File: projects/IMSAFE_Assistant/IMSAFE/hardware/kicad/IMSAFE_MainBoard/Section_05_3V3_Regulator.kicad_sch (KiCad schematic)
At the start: 0 parts

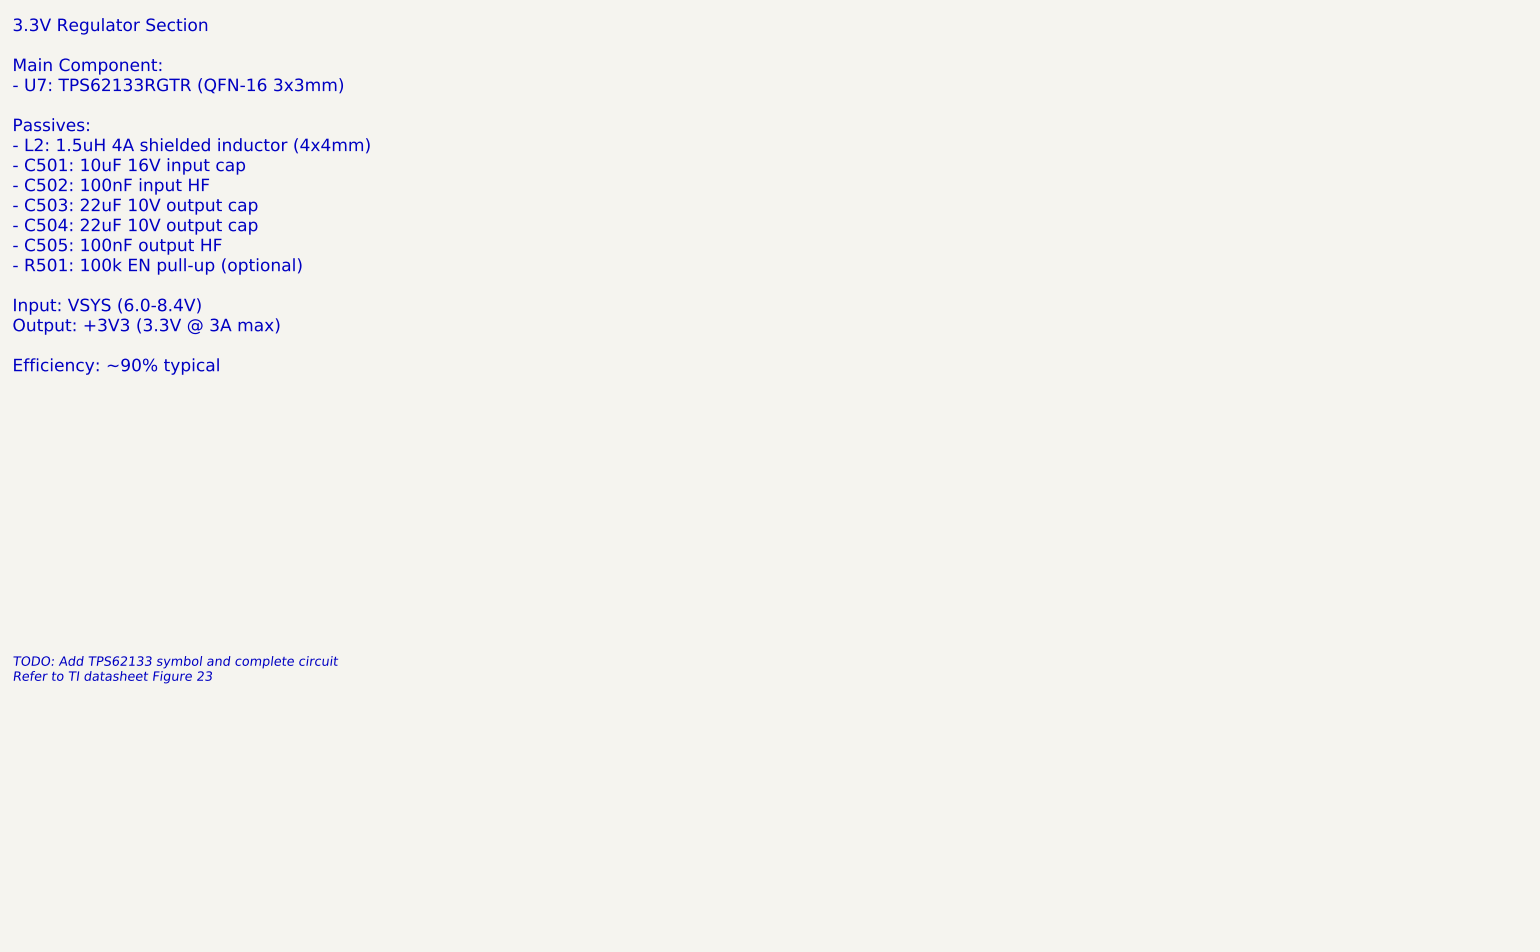
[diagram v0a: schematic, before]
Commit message: Add Sections 05-06: 3.3V and 5V buck regulators
Section 05 - TPS62133 (3.3V Fixed):
- 3A synchronous buck converter
- Input: VSYS (6-8.4V), Output: 3.3V
- Components: L2 (1.5µH), C501-C505, R501 (EN pull-up)
- Powers MCU and digital peripherals

Section 06 - TPS62130 (5V Adjustable):
- 3A synchronous buck converter with FB divider
- Input: VSYS, Output: 5.09V (R601=100k, R602=24.3k)
- Components: L3 (1.5µH), C601-C605, R601-R603
- Powers WS2812B LEDs, display, buzzer

Co-Authored-By: Claude Opus 4.5 <noreply@anthropic.com>
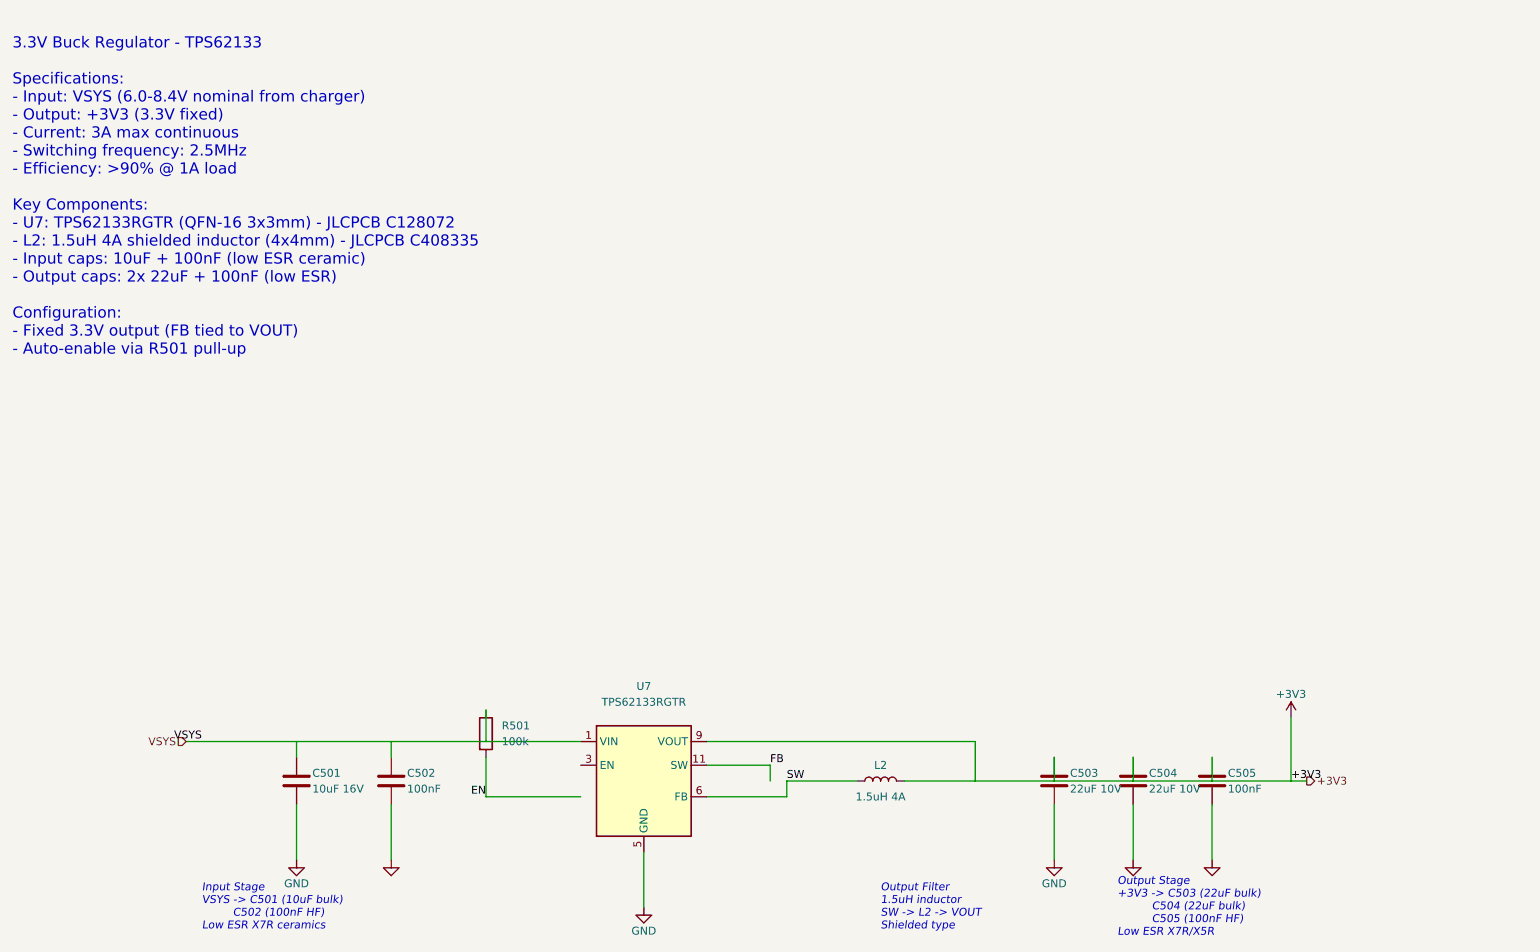
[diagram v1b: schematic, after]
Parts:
- added C501: 10uF 16V, Capacitor_SMD:C_0805_2012Metric, symbol Device:C
- added C502, C505: 100nF, Capacitor_SMD:C_0603_1608Metric, symbol Device:C
- added C503, C504: 22uF 10V, Capacitor_SMD:C_0805_2012Metric, symbol Device:C
- added L2: 1.5uH 4A, Inductor_SMD:L_4x4mm_H2.5mm, symbol Device:L
- added R501: 100k, Resistor_SMD:R_0603_1608Metric, symbol Device:R
- added U7: TPS62133RGTR, Package_DFN_QFN:QFN-16-1EP_3x3mm_P0.5mm_EP1.8x1.8mm, symbol Regulator:TPS62133RGTR
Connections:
- new net +3V3: C503.1, C504.1, C505.1, L2.2, U7.9 (VOUT)
- new net EN: R501.2
- new net FB: U7.11 (SW)
- new net GND: C501.2, C502.2, C503.2, C504.2, C505.2, U7.5 (GND)
- new net SW: L2.1, U7.6 (FB)
- new net VSYS: C501.1, C502.1, R501.1, U7.1 (VIN)
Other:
- note added: "3.3V Buck Regulator - TPS62133 Specifications: - Input: VSYS (6.0-8.4V nominal from charger) - Output: +3V3 (3.3V fixed) - Current: 3A max continuous - Switching frequency: 2.5MHz - Efficiency: >90% @ 1A load Key Components: - U7: TPS62133RGTR (QFN-16 3x3mm) - JLCPCB C128072 - L2: 1.5uH 4A shielded inductor (4x4mm) - JLCPCB C408335 - Input caps: 10uF + 100nF (low ESR ceramic) - Output caps: 2x 22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"
- note added: "Input Stage VSYS -> C501 (10uF bulk) C502 (100nF HF) Low ESR X7R ceramics"
- note added: "Output Filter 1.5uH inductor SW -> L2 -> VOUT Shielded type"
- note added: "Output Stage +3V3 -> C503 (22uF bulk) C504 (22uF bulk) C505 (100nF HF) Low ESR X7R/X5R"
- note removed: "3.3V Regulator Section Main Component: - U7: TPS62133RGTR (QFN-16 3x3mm) Passives: - L2: 1.5uH 4A shielded inductor (4x4mm) - C501: 10uF 16V input cap - C502: 100nF input HF - C503: 22uF 10V output cap - C504: 22uF 10V output cap - C505: 100nF output HF - R501: 100k EN pull-up (optional) Input: VSYS (6.0-8.4V) Output: +3V3 (3.3V @ 3A max) Efficiency: ~90% typical"
- note removed: "TODO: Add TPS62133 symbol and complete circuit Refer to TI datasheet Figure 23"

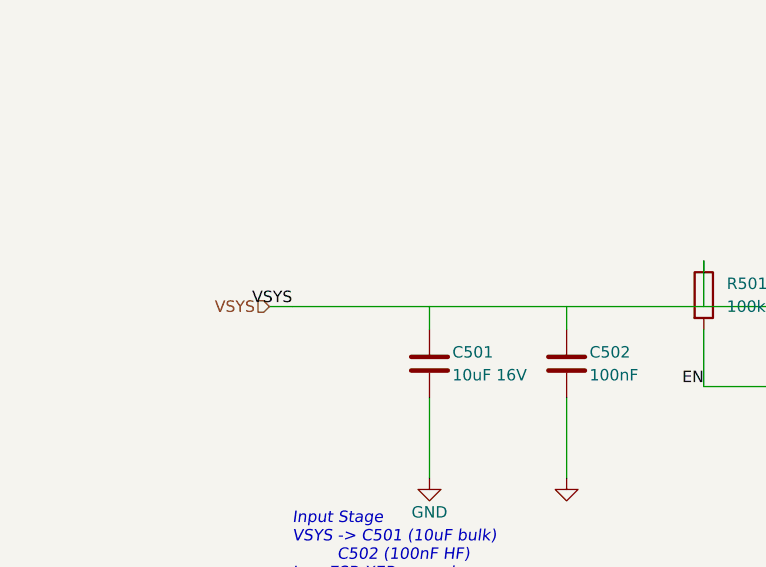
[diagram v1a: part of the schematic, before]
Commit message: Fix Section 06 FB divider for correct 5V output
- Change R602 from 24.3k to 19.1k (JLCPCB C25947)
- Corrects output voltage from 4.09V to 5.03V
- Update schematic text annotations with correct calculations
- Update design-rationale.md to reflect the fix
- Add PWR_FLAG symbols to Sections 04, 05, 06 for ERC compliance

Co-Authored-By: Claude Opus 4.5 <noreply@anthropic.com>
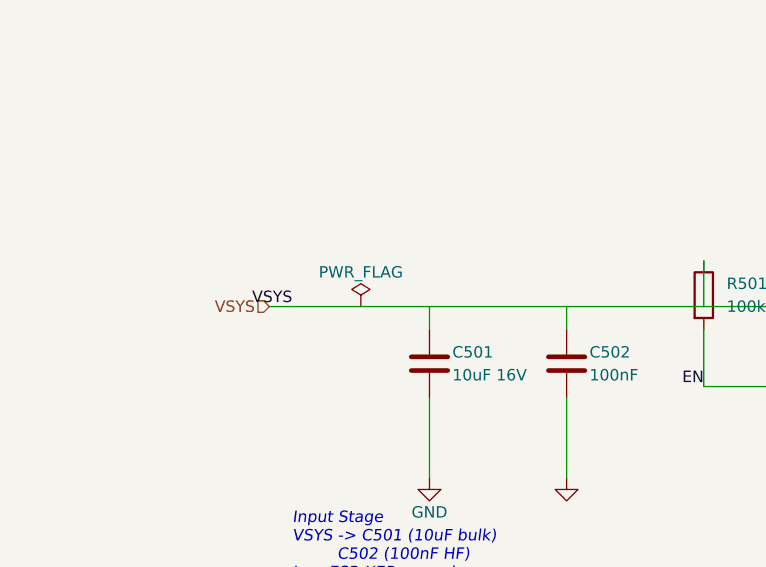
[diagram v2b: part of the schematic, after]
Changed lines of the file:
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@@
 	(wire (pts (xy 53.34 113.03) (xy 55.88 113.03)) (stroke (width 0) (type default)) (uuid "w-hl-vsys"))
 	(wire (pts (xy 231.14 119.38) (xy 233.68 119.38)) (stroke (width 0) (type default)) (uuid "w-hl-3v3"))
+	(symbol (lib_id "power:PWR_FLAG") (at 63.5 113.03 0) (unit 1)
+		(exclude_from_sim no) (in_bom yes) (on_board yes) (dnp no)
+		(uuid "pwr-flag-vsys")
+		(property "Reference" "#FLG0501" (at 63.5 111.125 0) (effects (font (size 1.27 1.27)) hide))
+		(property "Value" "PWR_FLAG" (at 63.5 109.22 0) (effects (font (size 1.27 1.27))))
+		(property "Footprint" "" (at 63.5 113.03 0) (effects (font (size 1.27 1.27)) hide))
+		(property "Datasheet" "~" (at 63.5 113.03 0) (effects (font (size 1.27 1.27)) hide))
+		(pin "1" (uuid "pwr-flag-vsys-p1"))
+		(instances (project "IMSAFE_MainBoard" (path "/sec05-0001-0002-0003-000000000001" (reference "#FLG0501") (unit 1))))
+	)
 	(sheet_instances (path "/" (page "1")))
 )

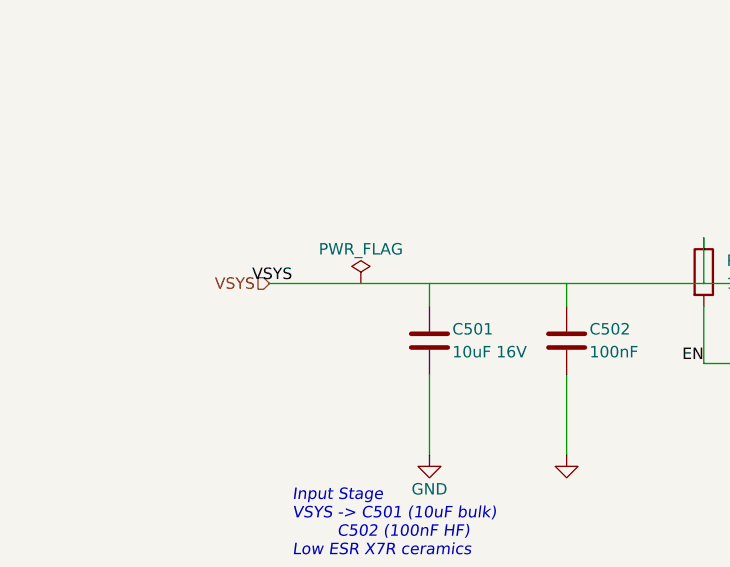
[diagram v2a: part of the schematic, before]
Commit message: Fix ERC errors across multiple schematic sections
- Section_04_BMS: Add VSYS hierarchical label for root schematic connection
- Section_05/06 Regulators: Add PWR_FLAG wire and junction to VSYS net
- Section_07_Barometric: Connect BMP390 SCK pin to GND for I2C mode
- Section_14_IO_Expander: Add no-connect symbols for unused MCP23017 GPIO pins
- Update design-rationale.md with ERC remediation status

Co-Authored-By: Claude Opus 4.5 <noreply@anthropic.com>
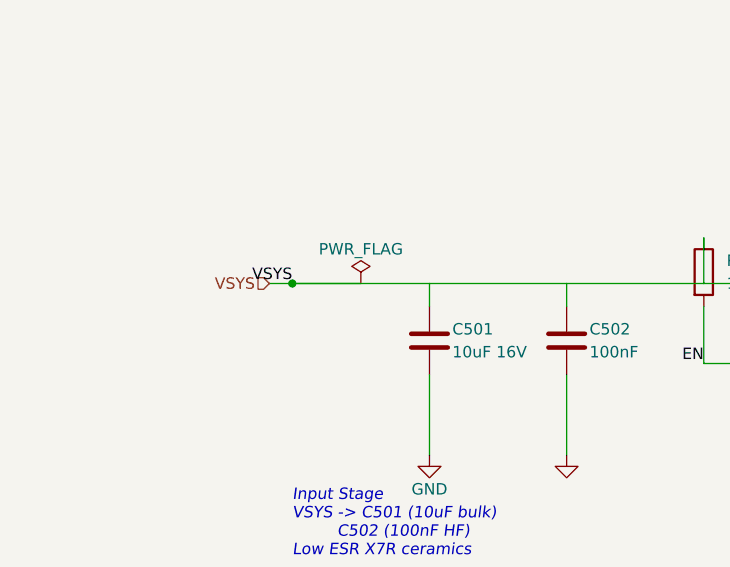
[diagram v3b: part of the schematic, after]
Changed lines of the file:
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@@
 	(wire (pts (xy 53.34 113.03) (xy 55.88 113.03)) (stroke (width 0) (type default)) (uuid "w-hl-vsys"))
 	(wire (pts (xy 231.14 119.38) (xy 233.68 119.38)) (stroke (width 0) (type default)) (uuid "w-hl-3v3"))
+	(wire (pts (xy 55.88 113.03) (xy 63.5 113.03)) (stroke (width 0) (type default)) (uuid "w-pwr-flag-vsys"))
+	(junction (at 55.88 113.03) (diameter 0) (color 0 0 0 0) (uuid "junction-vsys-main"))
 	(symbol (lib_id "power:PWR_FLAG") (at 63.5 113.03 0) (unit 1)
 		(exclude_from_sim no) (in_bom yes) (on_board yes) (dnp no)

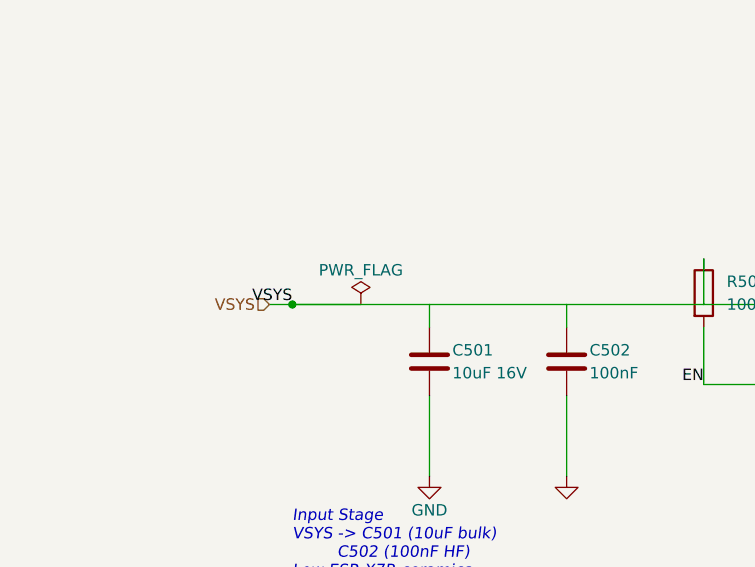
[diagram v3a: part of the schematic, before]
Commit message: Fix additional ERC errors in regulator and IO expander sections
- Section_05/06: Remove redundant PWR_FLAG on VSYS (BMS provides power_output)
- Section_14: Correct MCP23017 NC symbol positions to match actual pin coordinates

ERC reduction: 412 → 390 violations (22 fewer)
- Errors: 150 → 129 (-21)
- Warnings: 262 → 261 (-1)

Co-Authored-By: Claude Opus 4.5 <noreply@anthropic.com>
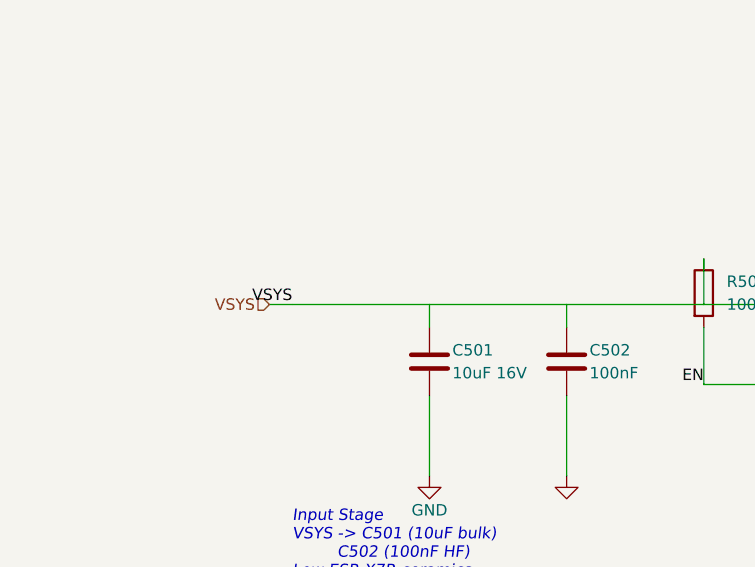
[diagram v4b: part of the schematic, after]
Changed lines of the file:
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@@
 	(wire (pts (xy 53.34 113.03) (xy 55.88 113.03)) (stroke (width 0) (type default)) (uuid "w-hl-vsys"))
 	(wire (pts (xy 231.14 119.38) (xy 233.68 119.38)) (stroke (width 0) (type default)) (uuid "w-hl-3v3"))
-	(wire (pts (xy 55.88 113.03) (xy 63.5 113.03)) (stroke (width 0) (type default)) (uuid "w-pwr-flag-vsys"))
-	(junction (at 55.88 113.03) (diameter 0) (color 0 0 0 0) (uuid "junction-vsys-main"))
-	(symbol (lib_id "power:PWR_FLAG") (at 63.5 113.03 0) (unit 1)
-		(exclude_from_sim no) (in_bom yes) (on_board yes) (dnp no)
-		(uuid "pwr-flag-vsys")
-		(property "Reference" "#FLG0501" (at 63.5 111.125 0) (effects (font (size 1.27 1.27)) hide))
-		(property "Value" "PWR_FLAG" (at 63.5 109.22 0) (effects (font (size 1.27 1.27))))
-		(property "Footprint" "" (at 63.5 113.03 0) (effects (font (size 1.27 1.27)) hide))
-		(property "Datasheet" "~" (at 63.5 113.03 0) (effects (font (size 1.27 1.27)) hide))
-		(pin "1" (uuid "pwr-flag-vsys-p1"))
-		(instances (project "IMSAFE_MainBoard" (path "/sec05-0001-0002-0003-000000000001" (reference "#FLG0501") (unit 1))))
-	)
 	(sheet_instances (path "/" (page "1")))
 )
